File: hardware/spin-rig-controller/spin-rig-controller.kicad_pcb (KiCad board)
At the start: 4 copper layers, 110 x 80 mm, 173 parts, among them J101 PACK IN, J102 BRAKE RES, J103 DRIVER PWR, J104 5V AUX, J201 USB4110GFA, J202 PI 4B, J203 QWIIC, J301 CL57T CONTROL, J302 ENCODER IN, J303 INDEX, J304 GNSS, J305 ENCODER OUT, Q101 NCE60P50K, Q102 AO4264E, SW201 BOOT, SW202 RESET, U101 INA238AIDGSR, U102 TLV3011AIDBVR, U103 UCC27517DBVR, U104 TPS54560BDDAR, U105 AP2112K-3.3TRG1, U201 ESP32-S3FN8, U301 SN74ACT244PWR, U302 AM26LV32EIDR, U303 SN74LVC1G17DBVR, U304 SN74LVC2G125DCTR, Y201 40 MHz

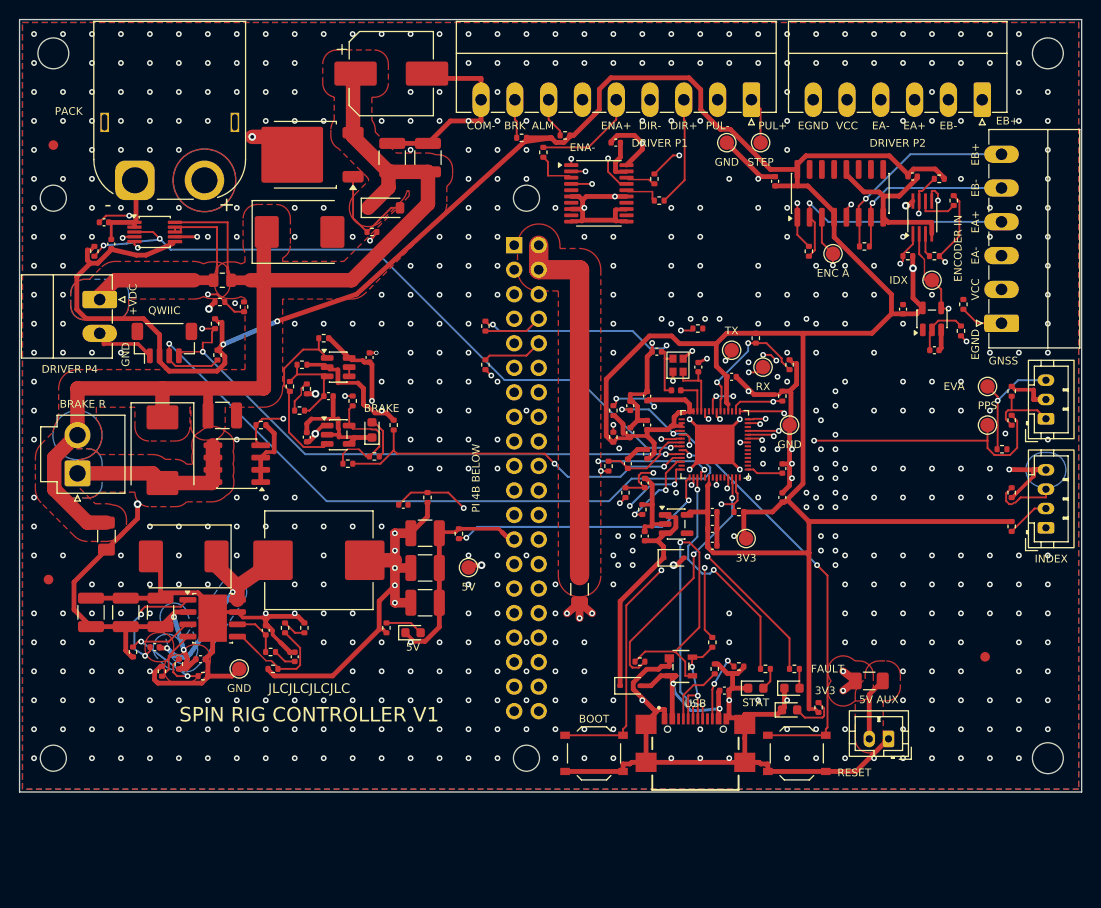
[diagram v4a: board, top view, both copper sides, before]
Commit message: hardware(spin-rig-controller): 67 x 90 mm over the Pi 4B -- covers the Pi but its port end, same connectors, one-sided 4-layer
The 110 x 80 board left a lot of empty copper. It now sits over the Pi on the
same 11 mm standoffs and the Pi's four M2.5 holes, with a 25 mm strip at the
top (XT60, input stage, encoder-out) and an 11 mm strip down the right (the
driver headers, index, GNSS) as the only overhang. Every connector and the
encoder pass-through stay; all SMD parts stay on the top side.

- design.py: the three M3 holes and the fiducials dropped (Economic
  assembly doesn't use them).
- make_pcb.py: new placement around U201_XY/U104_XY; the buck's BOOT/RT/EN
  runs and the ESP32's bottom fan-out are now locked pre-routes relative to
  those parts; In2's 5 V plane is the bottom 22 mm; Pi feed re-laid.
- fixup.py: the ESP32's 1.5 mm stitching grid follows U201_XY.
- silk.py: the title shrinks or turns to fit; pin labels and header names
  packed for the right edge.
- hand_fixes.py: re-planned for this routing result.
- README and FABRICATION-NOTES: 67 x 90, 540 vias, new pin-1 table and
  tooling-hole spots.

DRC 0 errors / 0 warnings / 0 unconnected, schematic parity clean, ERC 0
errors (the shared SP0503 symbol's 4 warnings), parity gate 167 symbols.

Co-Authored-By: Claude Opus 5.5 <noreply@anthropic.com>
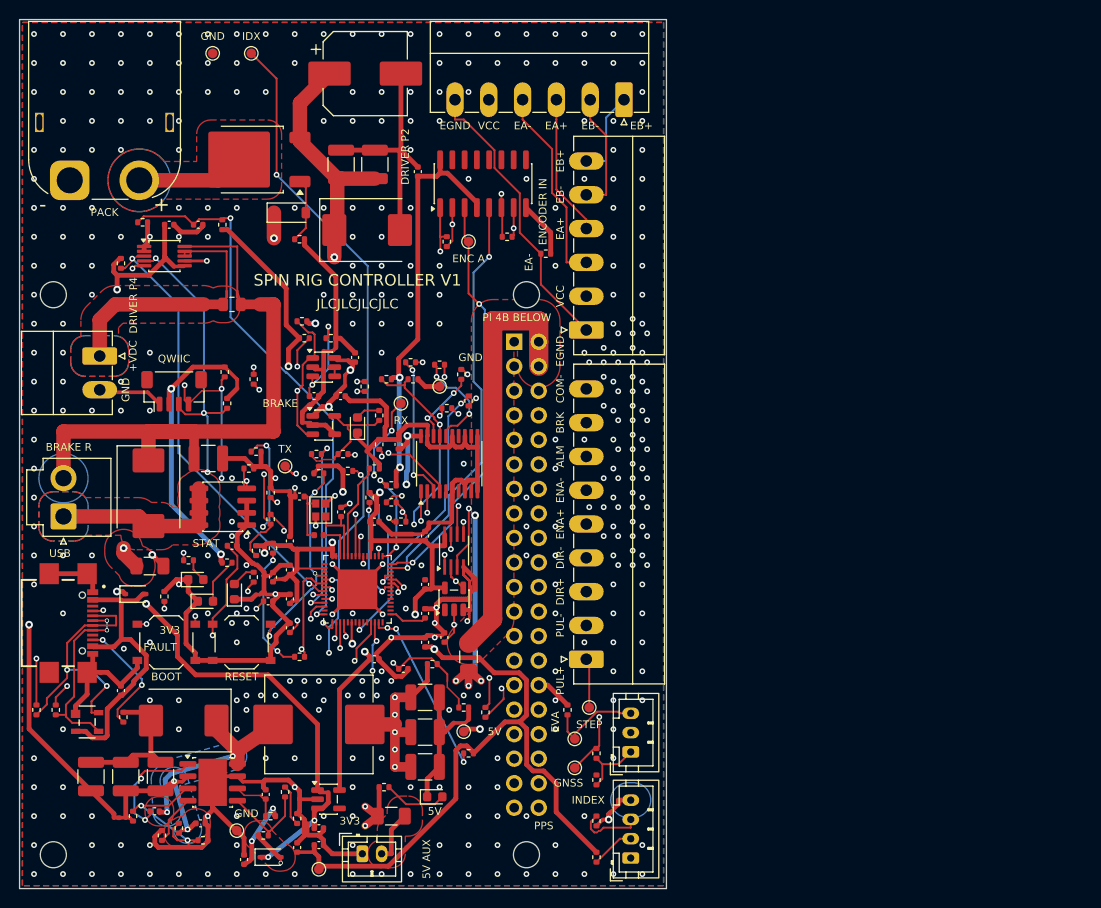
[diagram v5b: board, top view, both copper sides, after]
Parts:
- removed FID1, FID2, FID3: Fiducial, Fiducial:Fiducial_1mm_Mask2mm
- removed H1, H2, H4: M3, MountingHole:MountingHole_3.2mm_M3
- TP201, TP202, TP203, TP204, TP205, TP206, TP301, TP302, TP303, TP304, TP305, TP306: footprint TestPoint:TestPoint_Pad_D1.5mm -> TestPoint:TestPoint_Pad_D1.0mm
- moved TP305 74.3 mm to (124.0, 103.5)
- moved TP205 71.1 mm to (120.0, 103.5)
- moved R207 70.3 mm to (101.8, 171.5)
- moved R320 66.2 mm to (139.5, 152.0), turned to 0 degrees
- moved R323 65.0 mm to (138.5, 148.2)
- moved J201 64.4 mm to (106.5, 162.5), turned to -90 degrees
- moved R205 64.0 mm to (110.8, 172.2), turned to 90 degrees
- moved R210 63.8 mm to (117.5, 156.0)
- moved R319 63.1 mm to (148.2, 171.8)
- moved R208 63.1 mm to (121.5, 156.2), turned to 0 degrees
- moved D203 62.8 mm to (118.2, 158.0)
- moved C307 62.8 mm to (142.0, 153.5), turned to 90 degrees
- moved C212 62.5 mm to (110.5, 169.5), turned to 90 degrees
- moved CR201 61.8 mm to (107.0, 172.8)
- moved R321 61.8 mm to (138.5, 150.0)
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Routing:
- net +3V3: track 340.8 -> 278.6 mm, vias 4 -> 13
- net I2C_SDA: track 89.7 -> 50.6 mm, vias 3 -> 4
- net INDEX: track 35.9 -> 73.0 mm, vias 2 -> 3
- net +5V: track 153.8 -> 117.6 mm, vias 16 -> 19
- net /Driver and timing I/O/ALM_P: track 50.5 -> 85.0 mm, vias 1 -> 2
- net /Driver and timing I/O/PUL_P: track 18.1 -> 46.9 mm
- net /Power/VMAIN: track 106.8 -> 134.9 mm, vias 0 -> 3
- net INA_ALERT: track 73.6 -> 46.2 mm, vias 3 -> 2
- net /Power/VMAIN_F: track 80.1 -> 106.8 mm
- net /Power/V3V3_IN: track 23.2 -> 49.2 mm, vias 0 -> 4
- net STEP: track 48.7 -> 23.1 mm, vias 2 -> 3
- net /MCU/USB_DN_MCU: track 17.9 -> 42.6 mm
- net /MCU/USB_DP: track 43.3 -> 19.6 mm, vias 3 -> 2
- net VBUS_SENSE: track 80.1 -> 57.5 mm, vias 4 -> 2
- net DRV_OE_N: track 58.2 -> 35.9 mm, vias 2 -> 4
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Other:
- board size 110 x 80 mm -> 67 x 90 mm
- board text removed: "DRIVER P1"
